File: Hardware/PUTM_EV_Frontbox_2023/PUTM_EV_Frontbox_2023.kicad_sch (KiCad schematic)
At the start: 32 parts, among them J1 Złącze TE, J2 Conn_01x04, J3 Conn_02x14_Counter_Clockwise, J4 USB_C_Receptacle, J5 Conn_02x14_Counter_Clockwise, SW1 Reset switch, U1 STM32G473RCTx, U11 TLP291-4, U2 USBLC6-2P6

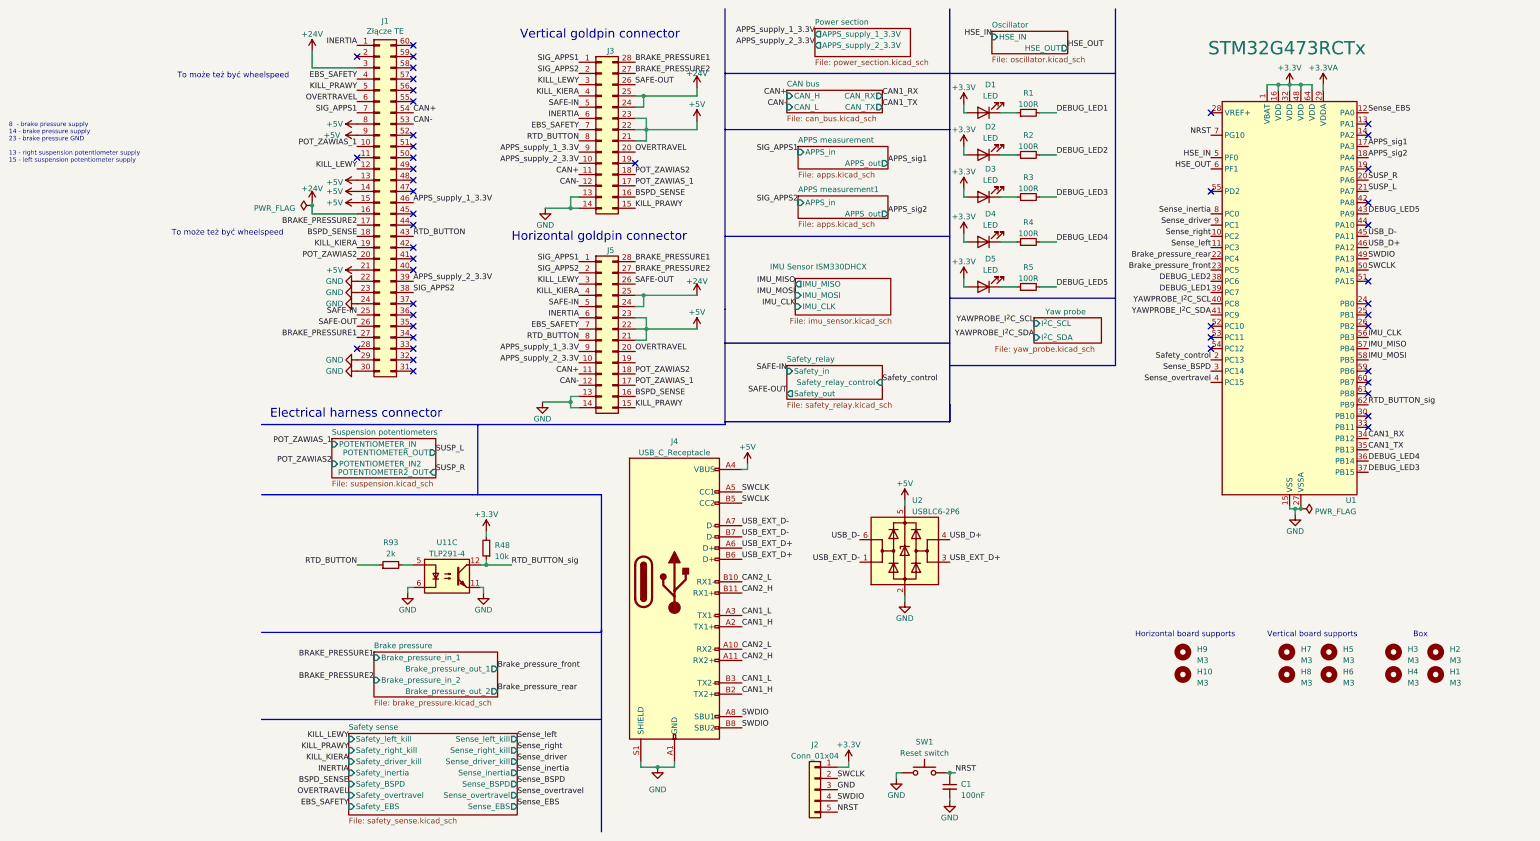
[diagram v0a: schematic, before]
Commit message: Redid component placement
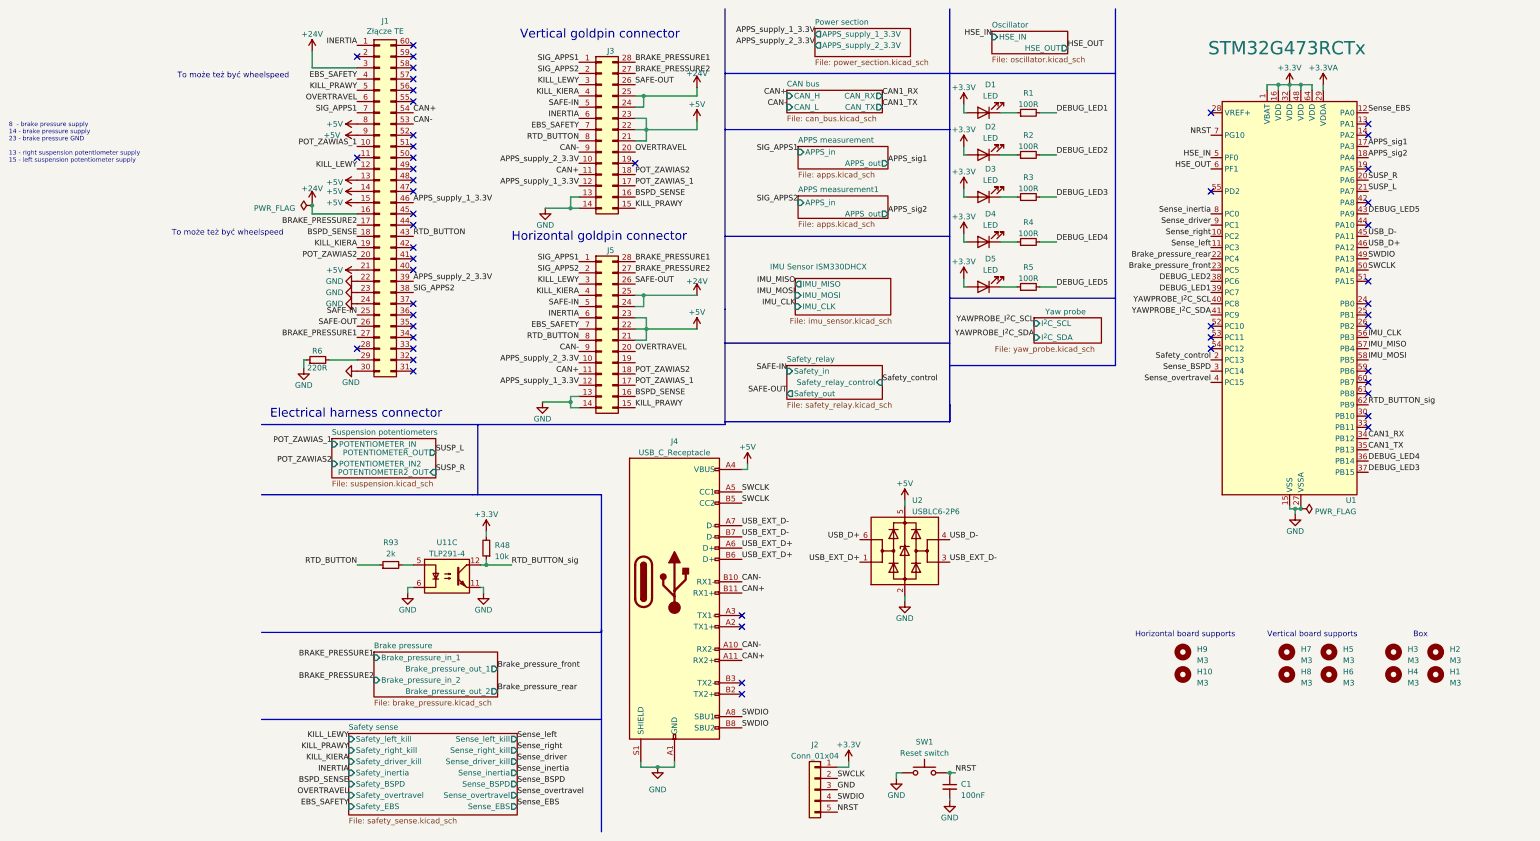
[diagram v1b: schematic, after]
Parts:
- added R6: 220R, Resistor_SMD:R_0402_1005Metric_Pad0.72x0.64mm_HandSolder, symbol Device:R_Small
- J2: footprint Connector_PinHeader_1.00mm:PinHeader_1x05_P1.00mm_Vertical -> Connector_PinHeader_2.54mm:PinHeader_1x05_P2.54mm_Vertical
- J4: footprint Connector_USB:USB_C_Receptacle_G-Switch_GT-USB-7010ASV -> Frontbox:CUI_UJ31-CH-31-SMT-TR
- J5: footprint Connector_PinSocket_2.54mm:PinSocket_2x14_P2.54mm_Horizontal -> Connector_PinSocket_2.54mm:PinSocket_2x14_P2.54mm_Vertical
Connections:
- net CAN2_H is gone; now on net CAN+: J4.A11 (RX2+), J4.B11 (RX1+)
- net CAN2_L is gone; now on net CAN-: J4.A10 (RX2-), J4.B10 (RX1-)
- net APPS_supply_1_3.3V: now also J3.12 (Pin_12), J5.12 (Pin_12); no longer J3.9 (Pin_9), J5.9 (Pin_9)
- net CAN-: now also J3.9 (Pin_9), J5.9 (Pin_9); no longer J3.12 (Pin_12), J5.12 (Pin_12)
- net GND: now also R6.1; no longer J1.29 (Pin_29)
- net USB_D+: now also U2.6 (I/O1); no longer U2.4 (I/O2)
- net USB_D-: now also U2.4 (I/O2); no longer U2.6 (I/O1)
- net USB_EXT_D+: now also U2.1 (I/O1); no longer U2.3 (I/O2)
- net USB_EXT_D-: now also U2.3 (I/O2); no longer U2.1 (I/O1)
- net CAN1_H: no longer names the net of J4.A2 (TX1+)
- net CAN1_H: no longer J4.B2 (TX2+)
- net CAN1_L: no longer names the net of J4.A3 (TX1-)
- net CAN1_L: no longer J4.B3 (TX2-)
- new net: J1.29 (Pin_29), R6.2
- no-connect marks 47 -> 51

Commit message: Finished most of the routing
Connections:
- net APPS_sig1: now also U1.18 (PA4); no longer U1.17 (PA3)
- net APPS_sig2: now also U1.17 (PA3); no longer U1.18 (PA4)
- net BRAKE_PRESSURE1: now also J3.27 (Pin_27); no longer J3.28 (Pin_28)
- net BRAKE_PRESSURE2: now also J3.28 (Pin_28); no longer J3.27 (Pin_27), J5.27 (Pin_27)
- net Brake_pressure_front: now also U1.22 (PC4); no longer U1.23 (PC5)
- net Brake_pressure_rear: now also U1.23 (PC5); no longer U1.22 (PC4)
- net RTD_BUTTON_sig: now also U1.3 (PC14); no longer U1.62 (PB9)
- net SUSP_L: now also U1.20 (PA6); no longer U1.21 (PA7)
- net SUSP_R: now also U1.21 (PA7); no longer U1.20 (PA6)
- net Safety_control: now also U1.12 (PA0); no longer U1.2 (PC13)
- net Sense_BSPD: now also U1.62 (PB9); no longer U1.3 (PC14)
- net Sense_EBS: now also U1.4 (PC15); no longer U1.12 (PA0)
- net Sense_driver: now also U1.10 (PC2); no longer U1.9 (PC1)
- net Sense_inertia: now also U1.11 (PC3); no longer U1.8 (PC0)
- net Sense_left: now also U1.8 (PC0); no longer U1.11 (PC3)
- net Sense_overtravel: now also U1.2 (PC13); no longer U1.4 (PC15)
- net Sense_right: now also U1.9 (PC1); no longer U1.10 (PC2)
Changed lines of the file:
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@@
     (effects (font (size 1.27 1.27)) (justify left bottom))
   )
-  (label "Sense_right" (at 226.695 63.5 180) (fields_autoplaced)
+  (label "Sense_right" (at 226.695 60.96 180) (fields_autoplaced)
     (effects (font (size 1.27 1.27)) (justify right bottom))
   )
@@
     (effects (font (size 1.27 1.27)) (justify right bottom))
   )
-  (label "Safety_control" (at 226.695 91.44 180) (fields_autoplaced)
-    (effects (font (size 1.27 1.27)) (justify right bottom))
+  (label "Safety_control" (at 262.255 35.56 0) (fields_autoplaced)
+    (effects (font (size 1.27 1.27)) (justify left bottom))
   )
   (label "POT_ZAWIAS_1" (at 33.655 43.18 180) (fields_autoplaced)
@@
     (effects (font (size 1.27 1.27)) (justify right bottom))
   )
-  (label "Sense_left" (at 226.695 66.04 180) (fields_autoplaced)
+  (label "Sense_left" (at 226.695 58.42 180) (fields_autoplaced)
     (effects (font (size 1.27 1.27)) (justify right bottom))
   )
@@
     (effects (font (size 1.27 1.27)) (justify left bottom))
   )
-  (label "APPS_sig2" (at 262.255 45.72 0) (fields_autoplaced)
+  (label "APPS_sig2" (at 262.255 43.18 0) (fields_autoplaced)
     (effects (font (size 1.27 1.27)) (justify left bottom))
   )
@@
     (effects (font (size 1.27 1.27)) (justify right bottom))
   )
-  (label "APPS_sig1" (at 262.255 43.18 0) (fields_autoplaced)
+  (label "APPS_sig1" (at 262.255 45.72 0) (fields_autoplaced)
     (effects (font (size 1.27 1.27)) (justify left bottom))
   )
@@
     (effects (font (size 1.27 1.27)) (justify left bottom))
   )
-  (label "Sense_overtravel" (at 226.695 96.52 180) (fields_autoplaced)
+  (label "Sense_overtravel" (at 226.695 91.44 180) (fields_autoplaced)
     (effects (font (size 1.27 1.27)) (justify right bottom))
   )
@@
     (effects (font (size 1.27 1.27)) (justify right bottom))
   )
-  (label "SUSP_R" (at 262.255 50.8 0) (fields_autoplaced)
+  (label "SUSP_R" (at 262.255 53.34 0) (fields_autoplaced)
     (effects (font (size 1.27 1.27)) (justify left bottom))
   )
@@
     (effects (font (size 1.27 1.27)) (justify right bottom))
   )
-  (label "Brake_pressure_rear" (at 226.695 68.58 180) (fields_autoplaced)
+  (label "Brake_pressure_rear" (at 226.695 71.12 180) (fields_autoplaced)
     (effects (font (size 1.27 1.27)) (justify right bottom))
   )
@@
     (effects (font (size 1.27 1.27)) (justify left bottom))
   )
-  (label "BRAKE_PRESSURE1" (at 96.52 24.13 0) (fields_autoplaced)
+  (label "BRAKE_PRESSURE1" (at 96.52 26.67 0) (fields_autoplaced)
     (effects (font (size 1.27 1.27)) (justify left bottom))
   )
@@
     (effects (font (size 1.27 1.27)) (justify right bottom))
   )
-  (label "Brake_pressure_front" (at 226.695 71.12 180) (fields_autoplaced)
+  (label "Brake_pressure_front" (at 226.695 68.58 180) (fields_autoplaced)
     (effects (font (size 1.27 1.27)) (justify right bottom))
   )
@@
     (effects (font (size 1.27 1.27)) (justify left bottom))
   )
-  (label "BRAKE_PRESSURE2" (at 96.52 26.67 0) (fields_autoplaced)
+  (label "BRAKE_PRESSURE2" (at 96.52 24.13 0) (fields_autoplaced)
     (effects (font (size 1.27 1.27)) (justify left bottom))
   )
@@
     (effects (font (size 1.27 1.27)) (justify right bottom))
   )
-  (label "BRAKE_PRESSURE2" (at 96.52 71.755 0) (fields_autoplaced)
+  (label "BRAKE_PRESSURE2" (at 55.88 80.645 0) (fields_autoplaced)
     (effects (font (size 1.27 1.27)) (justify left bottom))
   )
@@
     (effects (font (size 1.27 1.27)) (justify right bottom))
   )
-  (label "Sense_BSPD" (at 226.695 93.98 180) (fields_autoplaced)
-    (effects (font (size 1.27 1.27)) (justify right bottom))
+  (label "Sense_BSPD" (at 262.255 101.6 0) (fields_autoplaced)
+    (effects (font (size 1.27 1.27)) (justify left bottom))
   )
   (label "USB_EXT_D-" (at 120.65 128.905 0) (fields_autoplaced)
@@
     (effects (font (size 1.27 1.27)) (justify left bottom))
   )
-  (label "Sense_EBS" (at 262.255 35.56 0) (fields_autoplaced)
-    (effects (font (size 1.27 1.27)) (justify left bottom))
-  )
-  (label "RTD_BUTTON_sig" (at 262.255 101.6 0) (fields_autoplaced)
-    (effects (font (size 1.27 1.27)) (justify left bottom))
+  (label "Sense_EBS" (at 226.695 96.52 180) (fields_autoplaced)
+    (effects (font (size 1.27 1.27)) (justify right bottom))
+  )
+  (label "RTD_BUTTON_sig" (at 226.695 93.98 180) (fields_autoplaced)
+    (effects (font (size 1.27 1.27)) (justify right bottom))
   )
   (label "SWDIO" (at 142.24 191.135 0) (fields_autoplaced)
@@
     (effects (font (size 1.27 1.27)) (justify right bottom))
   )
-  (label "SUSP_L" (at 262.255 53.34 0) (fields_autoplaced)
+  (label "SUSP_L" (at 262.255 50.8 0) (fields_autoplaced)
     (effects (font (size 1.27 1.27)) (justify left bottom))
   )
@@
     (effects (font (size 1.27 1.27)) (justify right bottom))
   )
-  (label "Sense_inertia" (at 226.695 58.42 180) (fields_autoplaced)
+  (label "Sense_inertia" (at 226.695 66.04 180) (fields_autoplaced)
     (effects (font (size 1.27 1.27)) (justify right bottom))
   )
@@
     (effects (font (size 1.27 1.27)) (justify left bottom))
   )
-  (label "Sense_driver" (at 226.695 60.96 180) (fields_autoplaced)
-    (effects (font (size 1.27 1.27)) (justify right bottom))
-  )
+  (label "Sense_driver" (at 226.695 63.5 180) (fields_autoplaced)
+    (effects (font (size 1.27 1.27)) (justify right bottom))
+  )

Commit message: Ready for production
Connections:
- net BRAKE_PRESSURE1: now also J3.28 (Pin_28); no longer J3.27 (Pin_27)
- net BRAKE_PRESSURE2: now also J3.27 (Pin_27), J5.27 (Pin_27); no longer J3.28 (Pin_28)
- no-connect marks 51 -> 52
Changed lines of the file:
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@@
   (no_connect (at 226.695 35.56))
   (no_connect (at 46.355 50.8))
+  (no_connect (at 96.52 92.075))
   (no_connect (at 120.65 149.225))
   (no_connect (at 46.355 60.96))
@@
     (effects (font (size 1.27 1.27)) (justify left bottom))
   )
-  (label "BRAKE_PRESSURE1" (at 96.52 26.67 0) (fields_autoplaced)
+  (label "BRAKE_PRESSURE1" (at 96.52 24.13 0) (fields_autoplaced)
     (effects (font (size 1.27 1.27)) (justify left bottom))
   )
@@
     (effects (font (size 1.27 1.27)) (justify left bottom))
   )
-  (label "BRAKE_PRESSURE2" (at 96.52 24.13 0) (fields_autoplaced)
+  (label "BRAKE_PRESSURE2" (at 96.52 26.67 0) (fields_autoplaced)
     (effects (font (size 1.27 1.27)) (justify left bottom))
   )
@@
     (effects (font (size 1.27 1.27)) (justify right bottom))
   )
-  (label "BRAKE_PRESSURE2" (at 55.88 80.645 0) (fields_autoplaced)
+  (label "BRAKE_PRESSURE2" (at 96.52 71.755 0) (fields_autoplaced)
     (effects (font (size 1.27 1.27)) (justify left bottom))
   )
@@
           (reference "J4") (unit 1)
         )
+        (path "/b652b05a-4e3d-4ad1-b032-18886abe7d45/ba538a3c-1084-4770-aed2-08b4305d2379"
+          (reference "J4") (unit 1)
+        )

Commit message: Written firmware
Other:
- sheet APPS measurement1: file apps.kicad_sch -> apps1.kicad_sch
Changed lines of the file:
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@@
       (effects (font (size 1.27 1.27)) (justify left bottom))
     )
-    (property "Sheetfile" "apps.kicad_sch" (at 133.35 60.0206 0)
+    (property "Sheetfile" "apps1.kicad_sch" (at 133.35 60.0206 0)
       (effects (font (size 1.27 1.27)) (justify left top))
     )
+    (property "Field2" "" (at 133.35 54.356 0)
+      (effects (font (size 1.27 1.27)) hide)
+    )
     (pin "APPS_in" input (at 133.35 55.88 180)

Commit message: PCB taken apart
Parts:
- removed J1: Złącze TE, Frontbox:Autosport, symbol Connector_Generic:Conn_02x30_Counter_Clockwise
- removed J3: Conn_02x14_Counter_Clockwise, Connector_PinHeader_2.54mm:PinHeader_2x14_P2.54mm_Horizontal, symbol Connector_Generic:Conn_02x14_Counter_Clockwise
- removed J4: USB_C_Receptacle, Frontbox:CUI_UJ31-CH-31-SMT-TR, symbol Connector:USB_C_Receptacle
- removed R93: 2k, Resistor_SMD:R_0402_1005Metric, symbol Device:R_Small
- removed U11: TLP291-4, Package_SO:SOIC-16_4.55x10.3mm_P1.27mm, symbol Isolator:TLP291-4
- removed U2: USBLC6-2P6, Package_TO_SOT_SMD:SOT-666, symbol Power_Protection:USBLC6-2P6
- added R57, R58: 220R, symbol Device:R_Small
- R48: value 10k -> 220R; footprint Resistor_SMD:R_0402_1005Metric -> (none)
- R6: footprint Resistor_SMD:R_0402_1005Metric_Pad0.72x0.64mm_HandSolder -> (none)
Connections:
- net APPS_supply_1_3.3V is gone; now on net BRAKE_PRESSURE1: J5.12 (Pin_12)
- net APPS_supply_2_3.3V is gone; now on an unnamed net: J5.10 (Pin_10)
- net RTD_BUTTON is gone; now on net SAFE-IN: J5.8 (Pin_8)
- net SIG_APPS1 is gone; now on net BSPD_SENSE: J5.1 (Pin_1)
- net SIG_APPS2 is gone; now on net KILL_PRAWY: J5.2 (Pin_2)
- net +24V: now also J5.28 (Pin_28); no longer J5.24 (Pin_24), J5.25 (Pin_25)
- net +3.3V: now also J2.5 (Pin_5); no longer J2.1 (Pin_1), R48.2
- net +5V: now also J5.27 (Pin_27); no longer J5.21 (Pin_21), J5.22 (Pin_22), J5.23 (Pin_23)
- net BRAKE_PRESSURE1: no longer J5.28 (Pin_28)
- net BRAKE_PRESSURE2: now also J5.13 (Pin_13); no longer J5.27 (Pin_27)
- net BSPD_SENSE: no longer J5.16 (Pin_16)
- net CAN+: now also J5.23 (Pin_23); no longer J5.11 (Pin_11)
- net CAN-: now also J5.24 (Pin_24); no longer J5.9 (Pin_9)
- net GND: now also J5.25 (Pin_25), J5.26 (Pin_26), R57.2, R58.2; no longer J2.3 (Pin_3), J5.13 (Pin_13), J5.14 (Pin_14), R6.1
- net KILL_KIERA: now also J5.5 (Pin_5); no longer J5.4 (Pin_4)
- net KILL_LEWY: now also J5.4 (Pin_4); no longer J5.3 (Pin_3)
- net KILL_PRAWY: no longer J5.15 (Pin_15)
- net NRST: no longer J2.5 (Pin_5)
- net OVERTRAVEL: now also J5.3 (Pin_3); no longer J5.20 (Pin_20)
- net POT_ZAWIAS2: now also J5.14 (Pin_14); no longer J5.18 (Pin_18)
- net POT_ZAWIAS_1: now also J5.15 (Pin_15); no longer J5.17 (Pin_17)
- net RTD_BUTTON_sig: no longer R48.1
- net SAFE-IN: no longer J5.5 (Pin_5)
- net SAFE-OUT: now also J5.9 (Pin_9); no longer J5.26 (Pin_26)
- net SWCLK: no longer J2.2 (Pin_2)
- net SWDIO: no longer J2.4 (Pin_4)
- net DAC1_REF: now reaches U1.44 (PA10)
- net DAC2_REF: now reaches U1.52 (PC10)
- net at J5.19 (Pin_19): now also R57.1
- net USB_D+: no longer names the net of U1.46 (PA12)
- net USB_D-: no longer names the net of U1.45 (PA11)
- new net: J5.11 (Pin_11), R48.2
- new net: J5.18 (Pin_18), R58.1
- new net APPS1_3V3: R48.1
- new net APPS2_3V3: R6.1
- new net APPS_POT_1: J5.17 (Pin_17)
- new net APPS_POT_2: J5.16 (Pin_16)
- no-connect marks 52 -> 17
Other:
- removed sheet APPS measurement
- removed sheet APPS measurement1
- removed sheet Brake pressure
- added sheet APPS1 (APPS1.kicad_sch)
- added sheet APPS2 (APPS1.kicad_sch)
- added sheet Brake Pressure Left (brake_pressure.kicad_sch)
- added sheet Brake Pressure Right (brake_pressure.kicad_sch)
- note removed: "8 - brake pressure supply 14 - brake pressure supply 23 - brake pressure GND 13 - right suspension potentiometer supply 15 - left suspension potentiometer supply"
- note removed: "Electrical harness connector"
- note removed: "To może też być wheelspeed"
- note removed: "Vertical goldpin connector"
- moved on the sheet: J2, J5

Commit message: Merged branch new_apps
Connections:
- net +3.3V: now also J2.1 (Pin_1); no longer J2.5 (Pin_5)
- net GND: now also J2.3 (Pin_3)
- net NRST: now also J2.5 (Pin_5)
- net SWCLK: now also J2.2 (Pin_2)
- net SWDIO: now also J2.4 (Pin_4)
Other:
- moved on the sheet: C1, J2, SW1
